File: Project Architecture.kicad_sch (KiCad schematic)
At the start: 0 parts

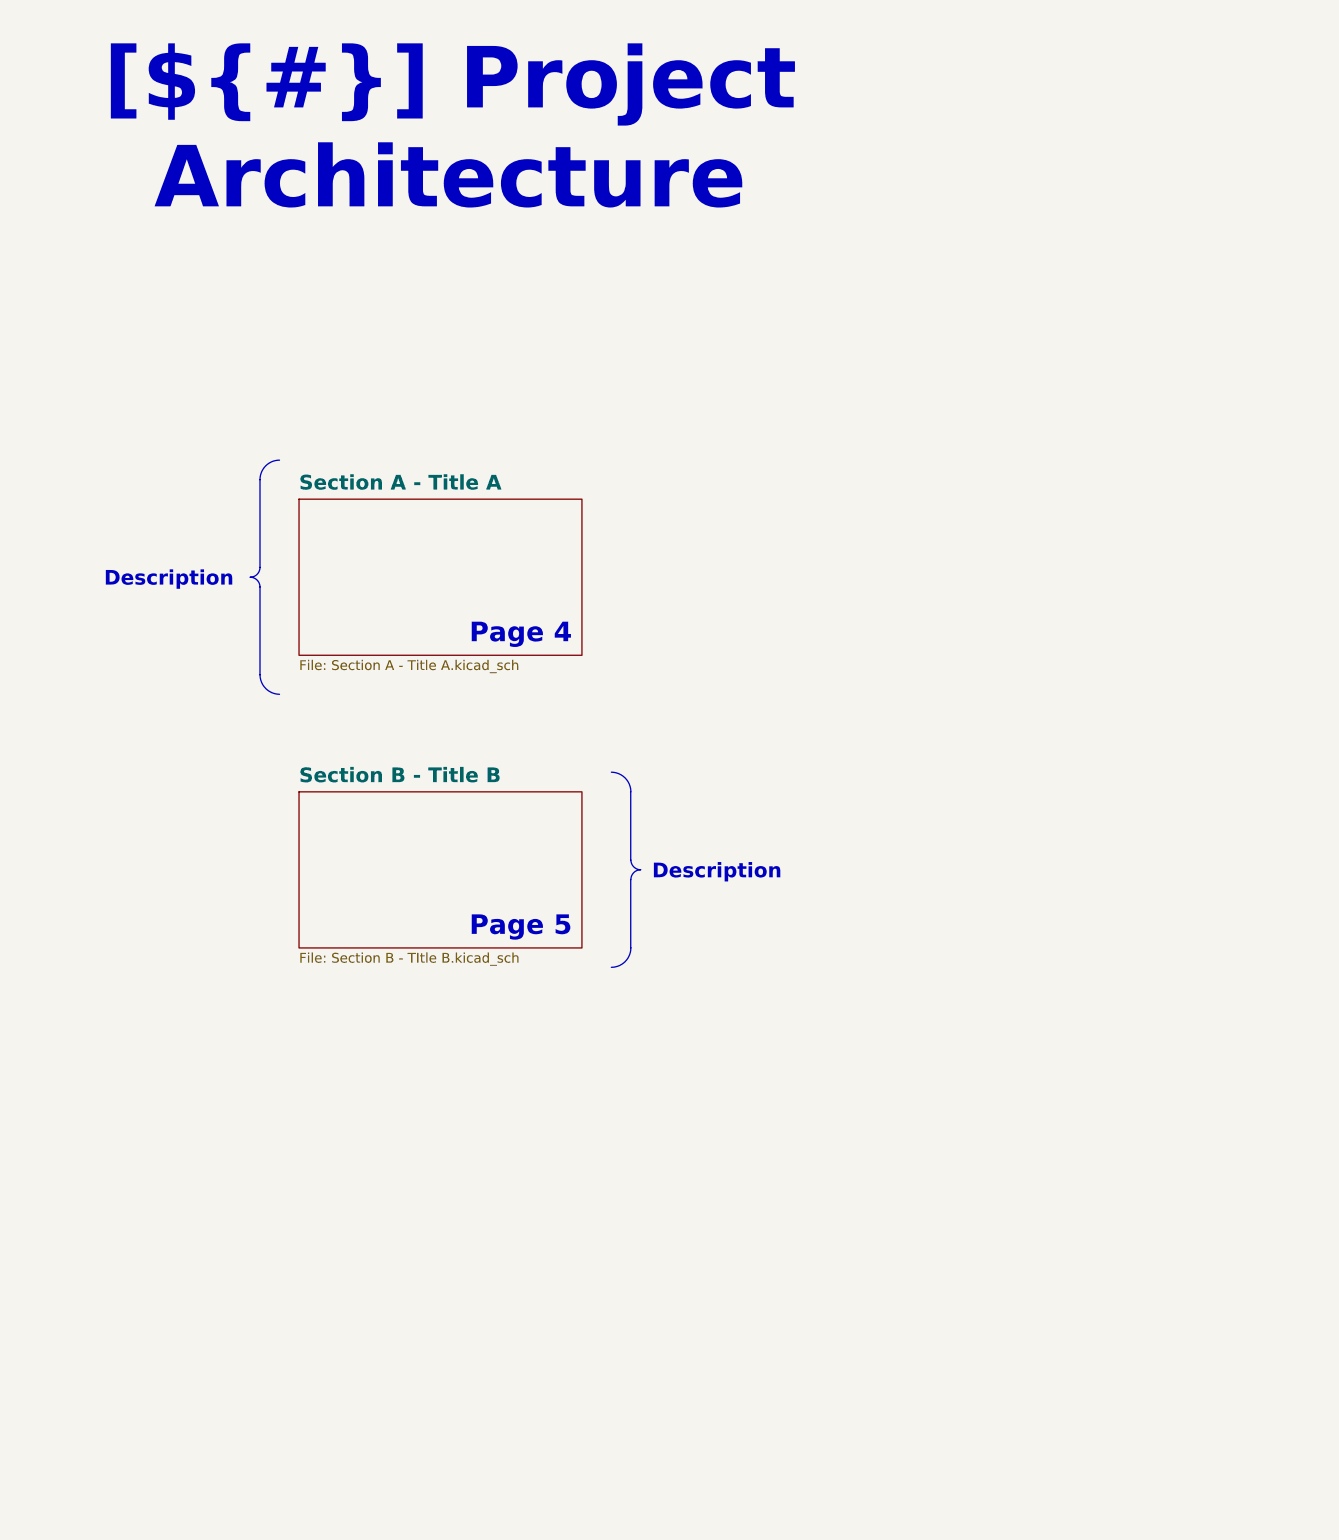
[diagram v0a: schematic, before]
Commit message: [Schematics] Merging changes from the initial project to the Template
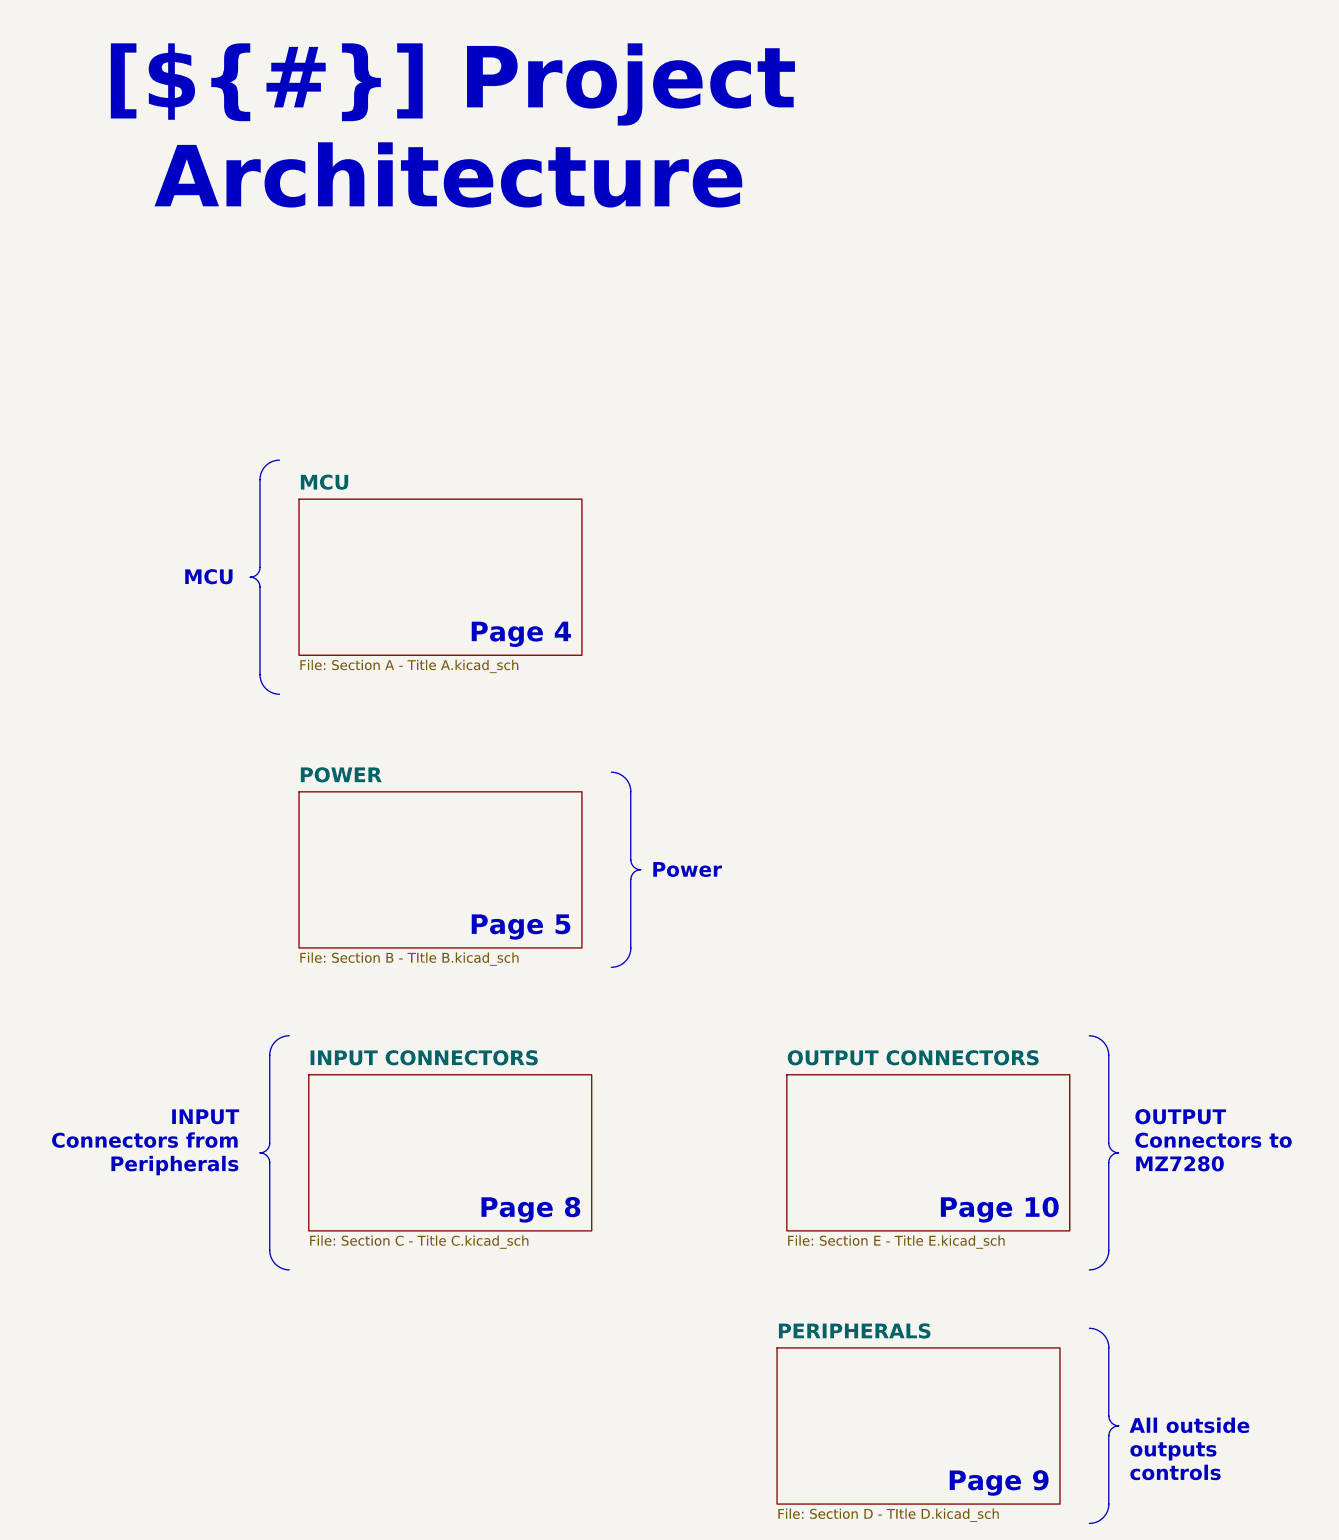
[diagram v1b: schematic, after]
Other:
- sheet Section A - Title A renamed MCU
- sheet Section B - Title B renamed POWER
- added sheet INPUT CONNECTORS (Section C - Title C.kicad_sch)
- added sheet OUTPUT CONNECTORS (Section E - Title E.kicad_sch)
- added sheet PERIPHERALS (Section D - TItle D.kicad_sch)
- note added: "Page 10"
- note added: "Page 8"
- note added: "Page 9"
